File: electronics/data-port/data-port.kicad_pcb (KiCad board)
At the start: 2 copper layers, 40 x 20 mm, 8 parts, among them J1 DATA, J2 LEAD, U1 USBLC6-2SC6

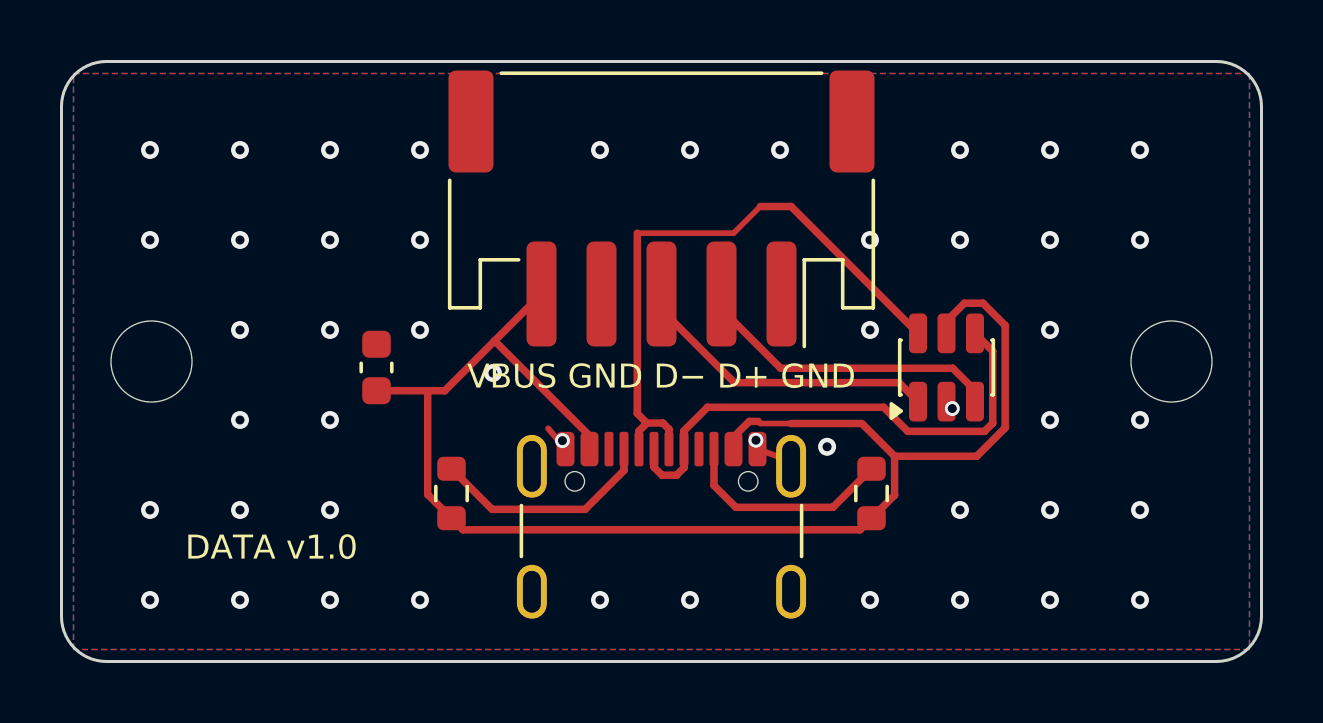
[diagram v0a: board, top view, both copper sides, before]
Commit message: DATA port board: 40 × 17, USB-C off-centre, to fit the drawer
The tray session's constraints for the board under the port wall:
- the right edge at most 9.5 mm right of the USB-C mouth (the chain
  foot's lock screw), the mouth staying where the DUT cables need it:
  the USB4105 at x 30.5 on a 40 mm board;
- at most 17 mm deep, for the PH plug and the wires' turn in the rear bay;
- both holes over the cable window, screwed from below: (3, 8.5) and
  (37.5, 4);
- the PH anywhere in [mouth − 26, mouth + 2]: x 17.5, not the proposed 21,
  since on a 17 mm board its courtyard and the USB4105's overlap in depth
  and must not in x.

Re-placed and re-routed.  ERC 0, DRC 0 / 0 unconnected / parity 0,
JLC DFM 0, 6 parts with a 3D model.  Docs and the BOM spec follow.

Co-Authored-By: Claude Opus 5.5 <noreply@anthropic.com>
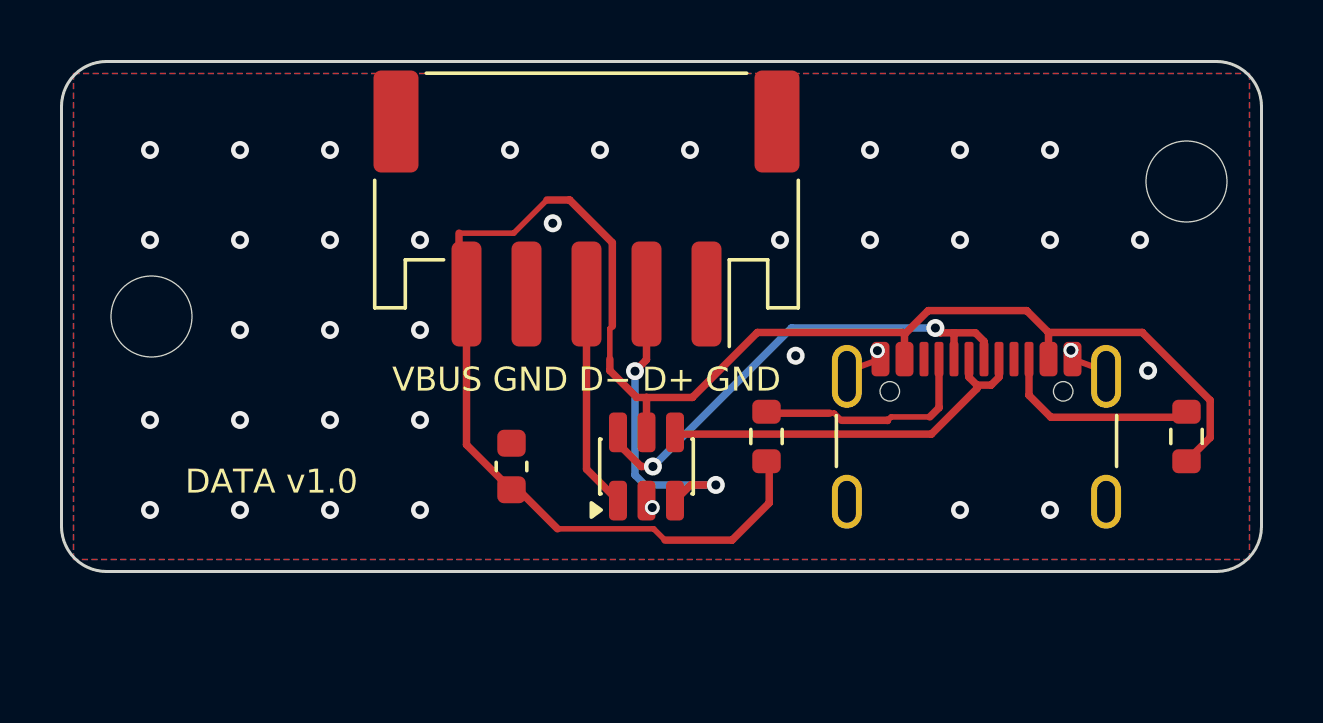
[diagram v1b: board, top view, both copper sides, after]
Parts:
- moved J1 10.9 mm to (30.5, 13.6)
- moved R1 10.7 mm to (23.5, 12.5)
- moved R2 10.7 mm to (37.5, 12.5)
- moved U1 10.5 mm to (19.5, 13.5)
- moved H2 6.02 mm to (37.5, 4.00)
- moved C1 5.58 mm to (15.0, 13.5)
- moved J2 2.50 mm to (17.5, 4.90)
- moved H1 1.50 mm to (3.00, 8.50)
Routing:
- net /Port/VBUS: track 49.9 -> 59.1 mm
- net /Port/CONN_DP: track 17.3 -> 13.3 mm
- net /Port/CONN_DN: track 20.4 -> 16.5 mm, vias 0 -> 2
- net /Port/LEAD_DN: track 10.3 -> 7.32 mm
- net GND: track 3.40 -> 4.10 mm, vias 48 -> 37
- net /Port/LEAD_DP: track 10.4 -> 10.6 mm, vias 0 -> 2
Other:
- board size 40 x 20 mm -> 40 x 17 mm

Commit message: DATA lead on 8 wires: node J7 a vertical PH 8 (USB, I²C, INT), data port J2 an S8B
Density decisions of 2026-10-19: the DATA lead becomes the camera's PH 8
"Same direction" type and also carries the node's I²C and an open-drain,
active-low INT (IO4, 10k pull-up, 1k at J7) for a later DATA ×4 board.

- Node: J7 B8B vertical by the right edge (J5's old slot), J5 AUX
  horizontal in the middle, AUX parts in a column between them.  J7 now
  taps the pair at J4's pads (DUT_CONN_*, behind U8's ESD like J4); the
  branch is hand-drawn in usb_hs_routes() on B.Cu under J4, since
  Freerouting found no room on U8's mux side.  ERC 0, DRC 0, parity 0,
  99 models.
- Data port: S8B, pins 1–3 open, PH at x 14.4, left hole (2.6, 13.5),
  one silkscreen label per pin.  ERC 0, DRC 0, parity 0.
- Pin map (README, check_pinmap: DATA_INT reserved), docs, cabling,
  BOM (one PH 8 lead type for DATA and camera, no B5B/S5B), SCAD config.

Co-Authored-By: Claude Opus 5.5 <noreply@anthropic.com>
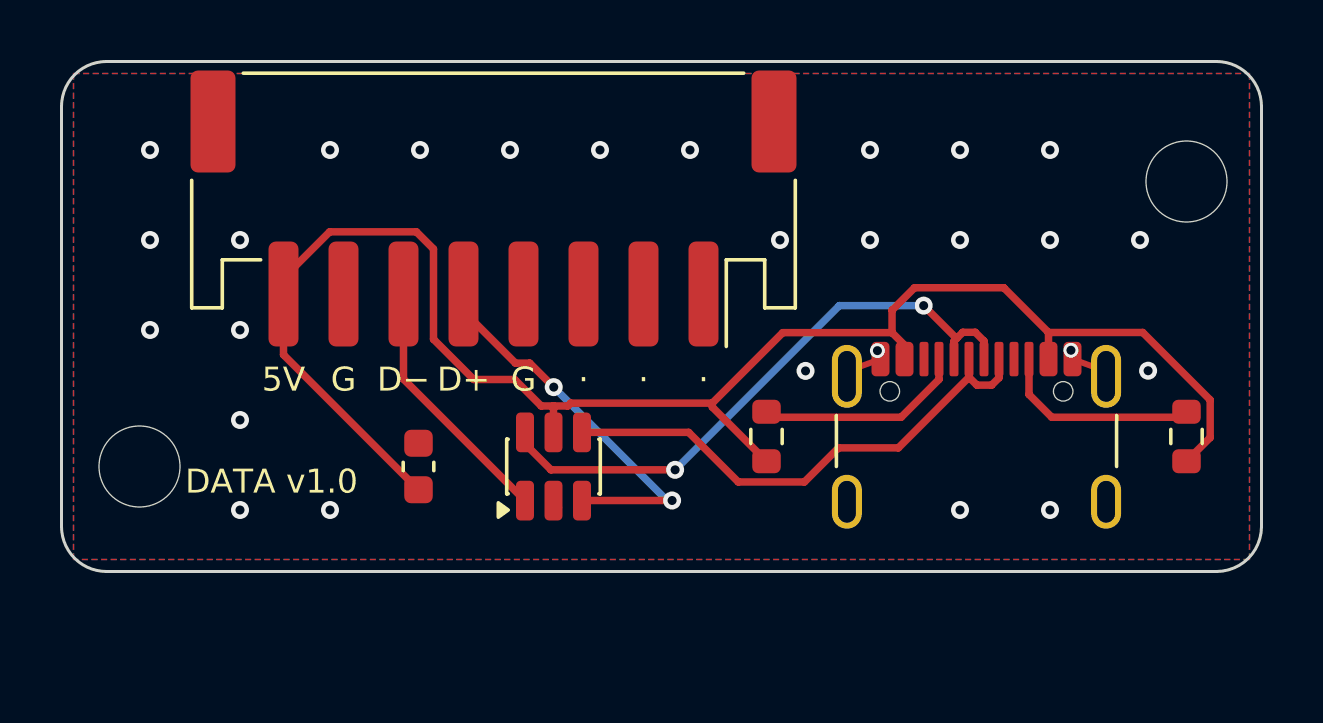
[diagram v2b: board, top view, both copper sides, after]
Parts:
- J2: footprint Connector_JST:JST_PH_S5B-PH-SM4-TB_1x05-1MP_P2.00mm_Horizontal -> Connector_JST:JST_PH_S8B-PH-SM4-TB_1x08-1MP_P2.00mm_Horizontal
- moved H1 5.02 mm to (2.60, 13.5)
- moved U1 3.10 mm to (16.4, 13.5)
- moved C1 3.10 mm to (11.9, 13.5)
- moved J2 3.10 mm to (14.4, 4.90)
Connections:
- J2 pad 1: GND -> unconnected-(J2-Pin_1-Pad1)
- J2 pad 2: /Port/LEAD_DP -> unconnected-(J2-Pin_2-Pad2)
- J2 pad 3: /Port/LEAD_DN -> unconnected-(J2-Pin_3-Pad3)
- J2 pad 5: /Port/VBUS -> /Port/LEAD_DP
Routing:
- net /Port/CONN_DP: track 13.3 -> 17.5 mm
- net /Port/CONN_DN: track 16.5 -> 20.3 mm
- net /Port/VBUS: track 59.1 -> 56.1 mm
- net /Port/LEAD_DP: track 10.6 -> 13.1 mm
- net /Port/LEAD_DN: track 7.32 -> 8.57 mm
- net /Port/CC1: track 7.67 -> 7.03 mm
- net GND: vias 37 -> 27
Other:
- board text added: "5V"
- board text added: "D+"
- board text added: "D−"
- board text added: "G"
- board text added: "·"
- board text removed: "VBUS GND D− D+ GND"

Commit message: Bay node: J7 takes D+ on pin 3, the DUT pair runs straight
U8 puts D- to the north and J7's side entry put D+ there, so D+ crossed
under D- on B.Cu.  The user chose to swap J7's pins 3/4 (3 D+, 4 D-):
DUT_CONN_DP/DN now run straight from U8 into J7, one 45° step each, no
via (14.6 / 14.7 mm; J3 -> J7 matched to ≈ 0.3 mm).

The data port follows through the lead (pin n <-> 9-n): J2 5 D-, 6 D+,
and U1's channels swap with it (D+ through 1/6), so every pad keeps the
copper it had.  Both boards re-routed: ERC 0, DRC 0, 0 unconnected,
parity 0, JLC READY.

The node's buck GND and +5V islands and the LDO tab are now exclusive
(0.5 mm), as on the hub: Freerouting cut buck-5v, then C12 off the LDO
tab.  Docs: electronics (HS path, J7 and lead pinouts), cabling, the
third Konnect round; BOM note.

Co-Authored-By: Claude Opus 5.5 <noreply@anthropic.com>
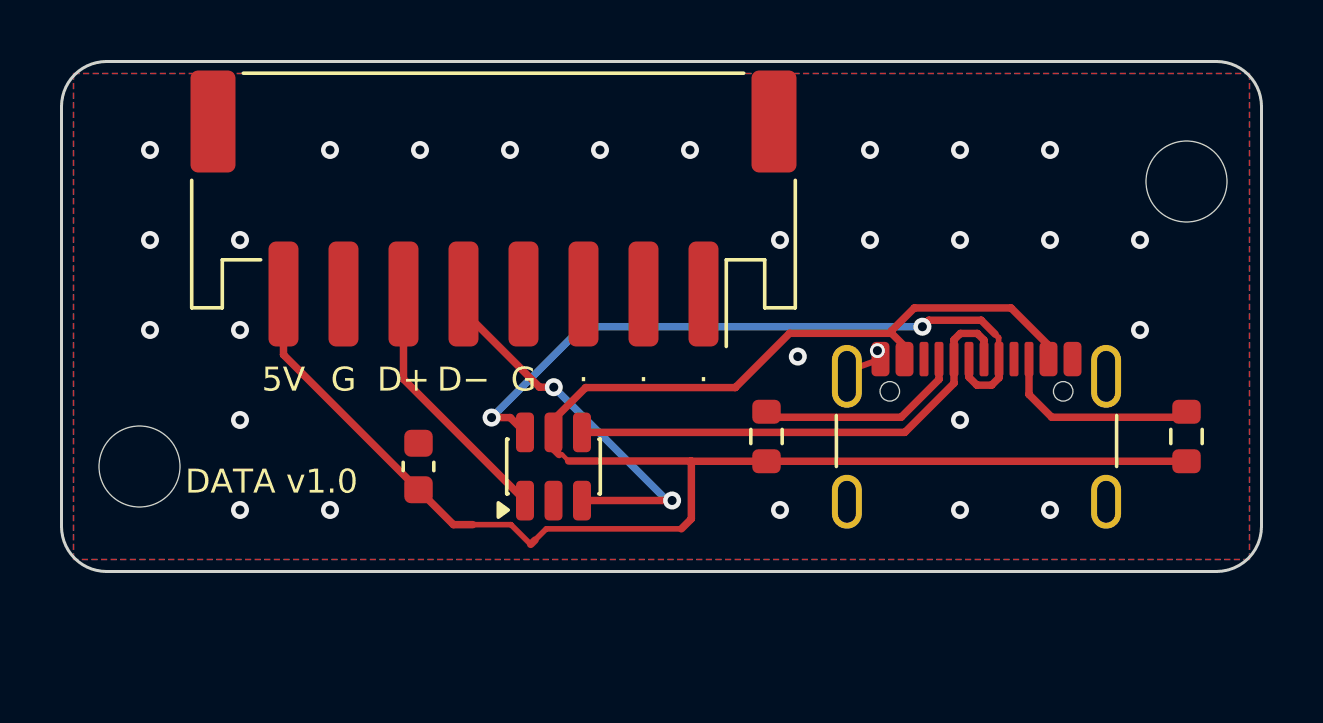
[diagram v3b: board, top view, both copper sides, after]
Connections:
- J2 pad 5: /Port/LEAD_DP -> /Port/LEAD_DN
- J2 pad 6: /Port/LEAD_DN -> /Port/LEAD_DP
- U1 pad 1: /Port/LEAD_DN -> /Port/LEAD_DP
- U1 pad 3: /Port/LEAD_DP -> /Port/LEAD_DN
- U1 pad 4: /Port/CONN_DP -> /Port/CONN_DN
- U1 pad 6: /Port/CONN_DN -> /Port/CONN_DP
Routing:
- net /Port/VBUS: track 56.1 -> 62.9 mm
- net /Port/CONN_DP: track 17.5 -> 23.0 mm, vias 0 -> 2
- net /Port/LEAD_DP: track 13.1 -> 8.57 mm, vias 2 -> 0
- net /Port/LEAD_DN: track 8.57 -> 13.1 mm, vias 0 -> 2
- net /Port/CONN_DN: track 20.3 -> 16.3 mm, vias 2 -> 0
- net GND: track 4.10 -> 1.90 mm, vias 27 -> 28

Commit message: DATA port: the PCBA review's fixes
D1: VBUS drawn, 0.8 mm F.Cu from J2.8 under the PH's housing into both of
J1's VBUS pad pairs, necked to 0.5 mm at the pad row (about 15 mOhm
instead of the routed 0.25 mm's 0.13 Ohm), in a Power netclass; thin
tracks to the Rp, C1 and the ESD's VBUS pin.  D2: 10 uF 0805 at the
receptacle (C2, a basic part).  D3: Rp 56k, "default USB power" as on
the DATA x4: 22k would advertise 1.5 A, above the node's TPS2553D low
end of 1.34 A.  D4: a meter check of each PH 8 lead in assembly.md.  D5:
checked in SolidCraft on B-rep (port wall with its U, board, USB4105, a
largest-size plug overmold): the mouth's 0.28 mm overhang sits inside
the U, 2.2 mm clear each side; the overmold clears it by 0.2 mm.

The CPL audit agrees on all 7 parts.  ERC 0, DRC 0, parity 0, 0
unconnected; the BOM follows.

Co-Authored-By: Claude Opus 5.5 <noreply@anthropic.com>
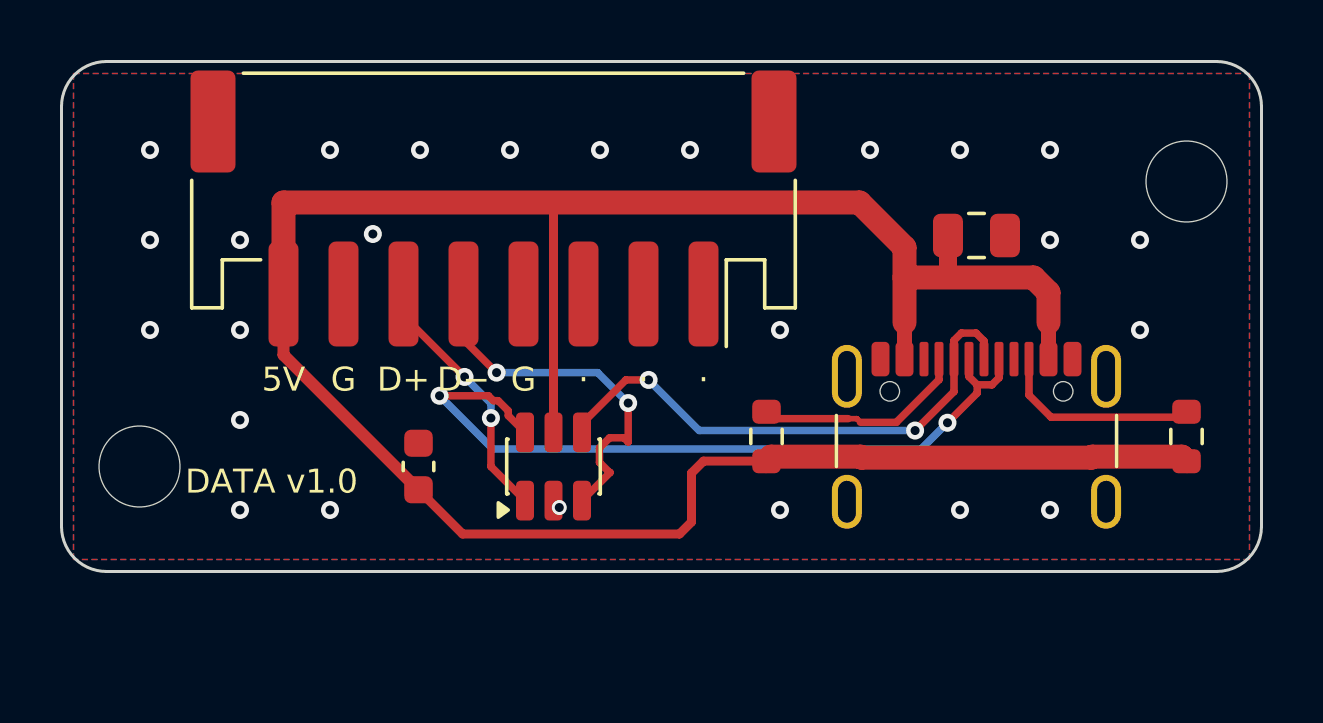
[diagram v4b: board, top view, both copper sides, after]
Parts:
- added C2: 10u, Capacitor_SMD:C_0805_2012Metric, F.Cu at (30.5, 5.80)
- R1, R2: value 22k -> 56k
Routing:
- net /Port/VBUS: track 62.9 -> 95.1 mm
- net /Port/CONN_DP: track 23.0 -> 25.6 mm
- net /Port/CONN_DN: track 16.3 -> 18.0 mm, vias 0 -> 2
- net GND: track 1.90 -> 0.30 mm, vias 28 -> 25
- net /Port/LEAD_DN: track 13.1 -> 12.6 mm
- net /Port/LEAD_DP: vias 0 -> 2

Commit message: Power pads connect solid on the DATA ×4, the DATA port and the camera pod
The rule from d58f976, applied to the three boards. Each one declares its power nets in design.py:
- DATA ×4: GND, +5V, each port's 5V_SW and VBUS
- DATA port: GND, VBUS
- camera pod: GND, CAM_5V
pcbgen then connects their IC and connector pins solid to the pours. A small part with an end on a
track keeps its reliefs. The .kicad_dru carries both rules.

Now solid:
- DATA ×4: the four receptacles' and J1's GND pins; the hub's, expanders', INA226s', switches' and
  ESDs' GND pins and exposed pads; the LDO's VIN, EN and GND on its islands. Eighteen GND pads the
  pour didn't reach (USB4105 A1/A12/B1/B12 among them) now take it directly, and their tie tracks go
  (25 segments, 11 vias). The ports' 5V_SW and VBUS run in tracks, so their pads don't change.
- DATA port: J1's four GND pins, J2's two, the ESD's GND.
- Camera pod: J1's two GND pins, J2's GND, the AMS1117's GND.

Worst relieved power-net pad, before → after:
- DATA ×4: INA226 GND (U102.7) on 1 spoke, 0.29 mm → solid. Now the worst is a GND decoupling cap or
  pull-down (C201.2, R201.2...) on 1 spoke of 0.40 mm, a signal-level current.
- DATA port: J1's GND pins and U1.2 on 1 spoke, 0.40 mm → solid. Now the worst is C1 / C2 / the shell
  tabs on 3 spokes, 1.20 mm.
- Camera pod: U1.1, J1.5 / J1.7, C1, C3 on 3 spokes, 1.20 mm. Now U1.1 and J1's GND are solid; the
  worst is C1 / C3 on 3 spokes, 1.20 mm.

Same routes re-imported: only GND ties and stitching vias move. ERC/DRC 0, parity 0, 0 unconnected on
all three. CPL and BOM unchanged, so the CPL audit stands. Renders, PDFs and gerbers regenerated.

Co-Authored-By: Claude Opus 5.5 <noreply@anthropic.com>
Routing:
- net GND: track 0.30 -> 0.00 mm, vias 25 -> 26
